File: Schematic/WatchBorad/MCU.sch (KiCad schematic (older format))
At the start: 54 parts, among them J2 Conn_01x07_Female, J3 Conn_01x12, U1 BNO055, U2 nRF52832-QFxx, U3 CAT4002ATD-GT3, U4 MX25R1635F, X1 Crystal_GND24_Small, X2 Crystal_Small, X3 Crystal_Small

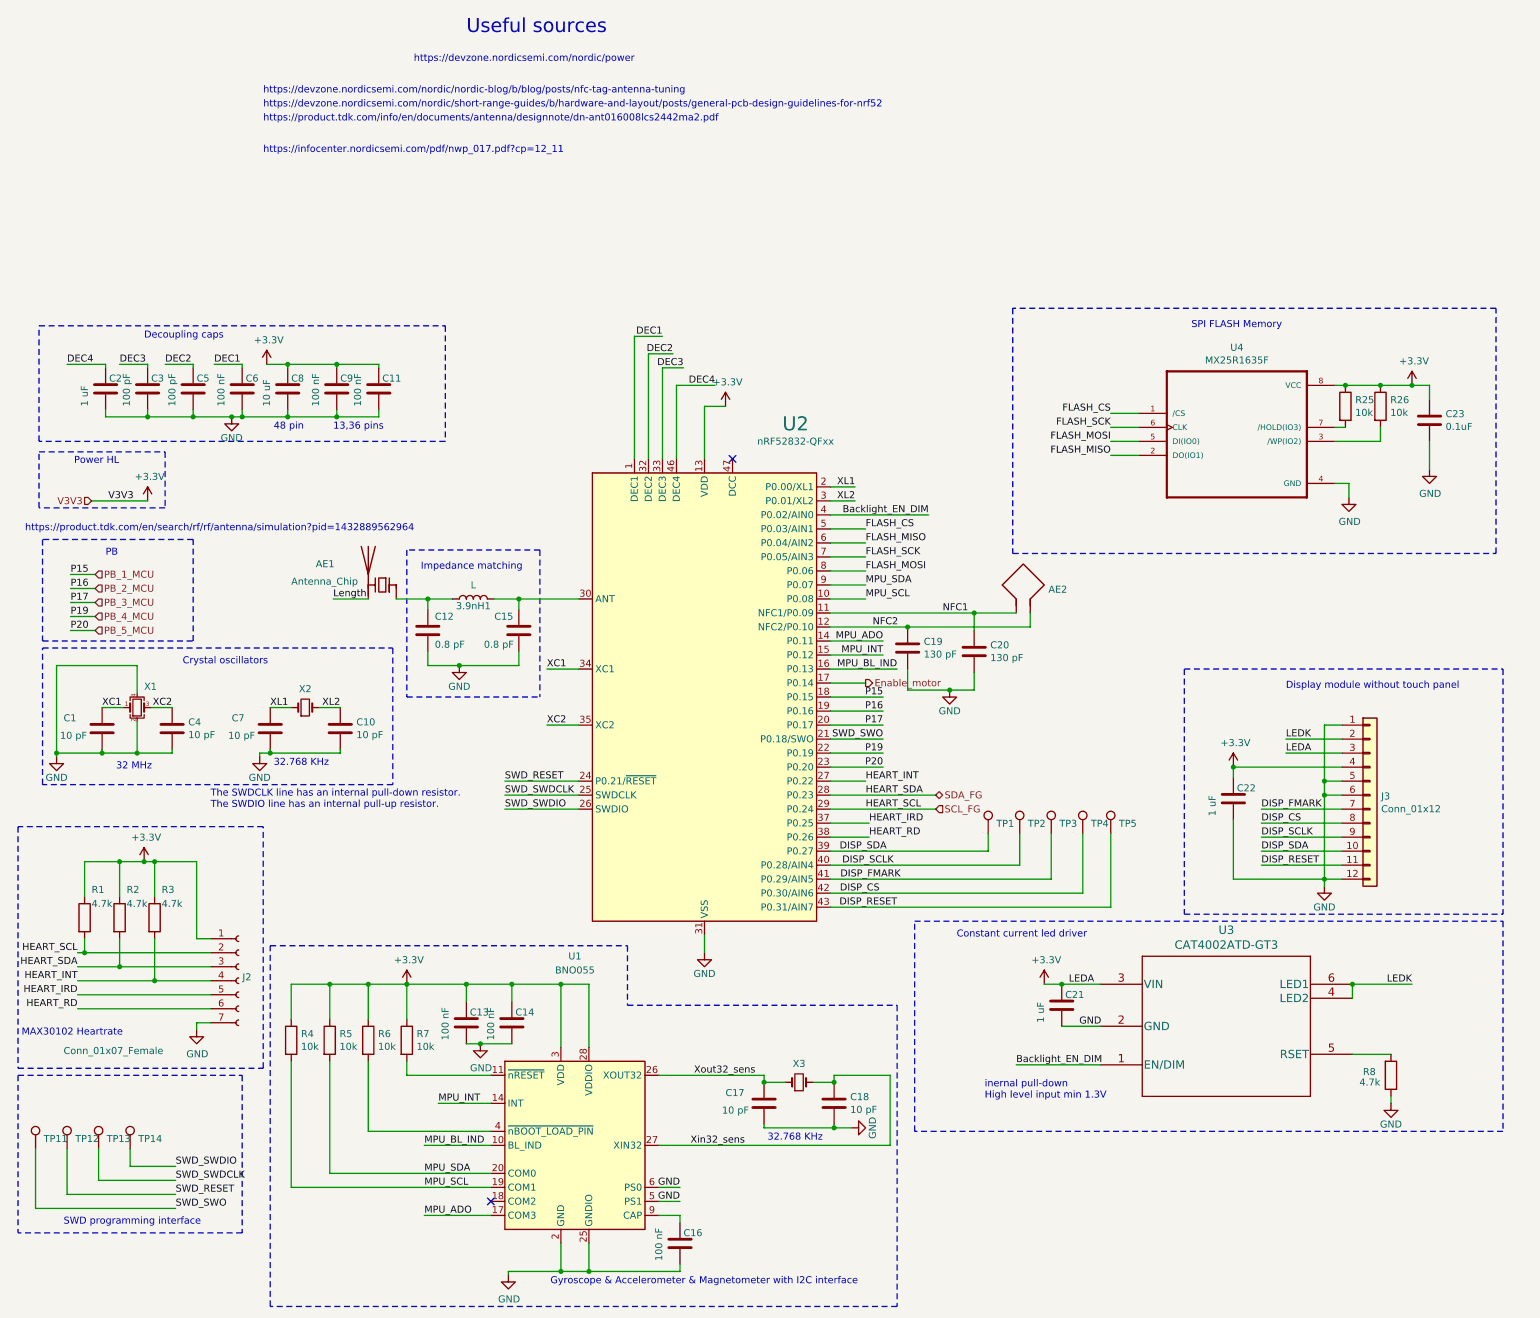
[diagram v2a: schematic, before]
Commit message: PBs are modified to one logic. Some minot changes
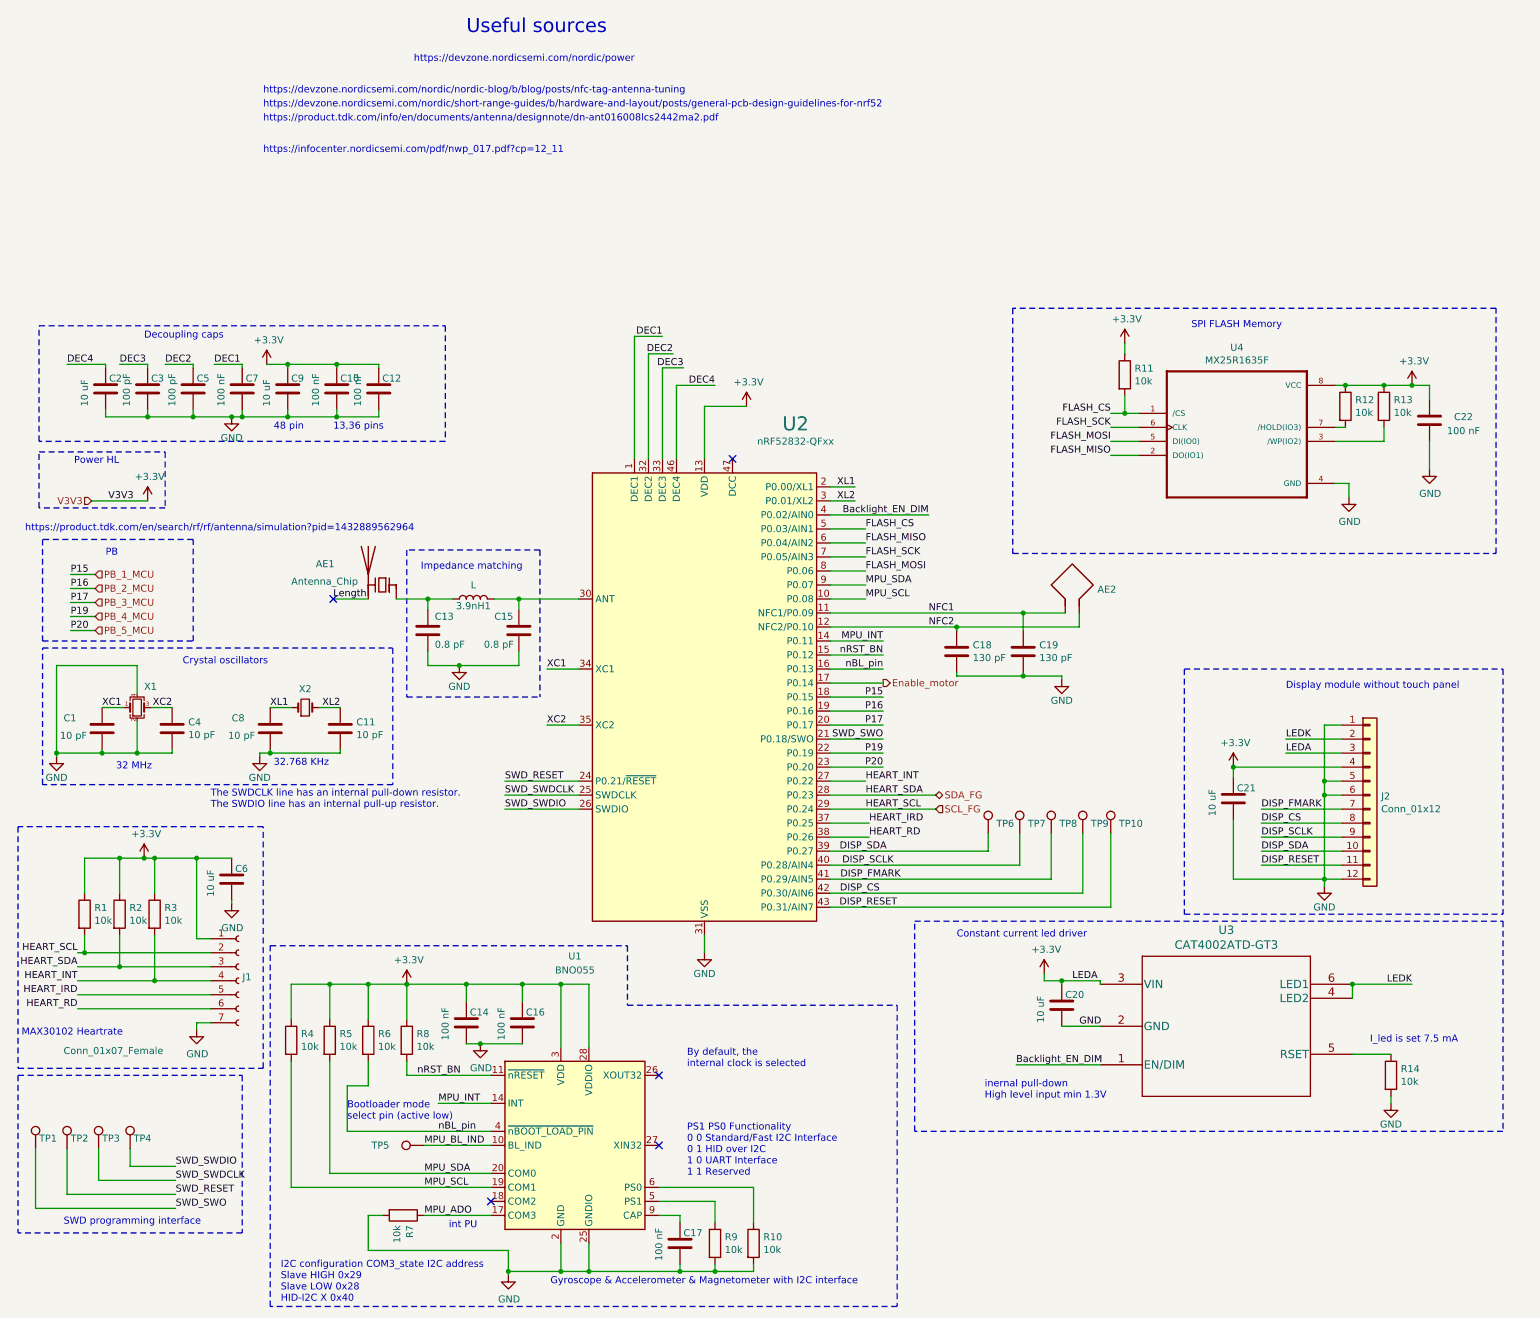
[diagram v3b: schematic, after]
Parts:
- removed C17, C18: 10 pF, Capacitors_SMD:C_0603_HandSoldering, symbol Device:C
- removed C23: 0.1uF, Capacitors_SMD:C_0603_HandSoldering, symbol Device:C
- removed R8: 4.7k, Resistors_SMD:R_0603_HandSoldering, symbol Device:R
- removed X3: Crystal_Small, Crystals:Crystal_SMD_2012-2pin_2.0x1.2mm, symbol Device:Crystal_Small
- added C20, C6: 10 uF, Capacitors_SMD:C_0603_HandSoldering, symbol Device:C
- added R10, R11, R14, R7, R9: 10k, Resistors_SMD:R_0603_HandSoldering, symbol Device:R
- added TP5: TestPoint, Measurement_Points:Measurement_Point_Round-SMD-Pad_Small, symbol Connector:TestPoint
- C2, C21: value 1 uF -> 10 uF; LCSC https://lcsc.com/product-detail/Multilayer-Ceramic-Capacitors-MLCC-SMD-SMT_SANYEAR-C0603X5R105K160NT_C475249.html -> https://lcsc.com/product-detail/Multilayer-Ceramic-Capacitors-MLCC-SMD-SMT_SANYEAR-C0603X5R106M160NT_C466781.html
- C22: value 1 uF -> 100 nF; LCSC https://lcsc.com/product-detail/Multilayer-Ceramic-Capacito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 -> (none)
- R1, R2, R3: value 4.7k -> 10k
- renumbered C9 to C10, C10 to C11, C11 to C12, C12 to C13, C13 to C14, C14 to C16, C16 to C17, C19 to C18, C20 to C19, C6 to C7, C7 to C8, C8 to C9, J2 to J1, J3 to J2, R25 to R12, R26 to R13, R7 to R8, TP11 to TP1, TP5 to TP10, TP12 to TP2, TP13 to TP3, TP14 to TP4, TP1 to TP6, TP2 to TP7, TP3 to TP8, TP4 to TP9
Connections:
- net +3V3: now also C20.1, C6.1, R11.1
- net FLASH_CS: now also R11.2
- net GND: now also C20.2, C6.2, R10.2, R14.2, R7.2, R9.2; no longer U1.5 (PS1), U1.6 (PS0)
- net MPU_ADO: now also R7.1; no longer U2.14 (P0.11)
- net MPU_BL_IND: now also TP5.1; no longer U2.16 (P0.13)
- net MPU_INT: now also U2.14 (P0.11); no longer U2.15 (P0.12)
- net at U3.5 (RSET): now also R14.1
- net nRST_BN: now reaches R8.2, U1.11 (~nRESET)
- net nRST_BN: now also U2.15 (P0.12)
- net nBL_pin: now reaches R6.2, U1.4 (~nBOOT_LOAD_PIN)
- net nBL_pin: now also U2.16 (P0.13)
- net Xin32_sens: no longer names the net of U1.27 (XIN32)
- net Xout32_sens: no longer names the net of U1.26 (XOUT32)
- new net: R9.1, U1.5 (PS1)
- new net: R10.1, U1.6 (PS0)
- no-connect marks 2 -> 5
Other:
- note added: "Bootloader mode\nselect pin (active low)"
- note added: "By default, the\ninternal clock is selected"
- note added: "I2C configuration COM3_state I2C address\nSlave HIGH 0x29\nSlave LOW 0x28\nHID-I2C X 0x40\n"
- note added: "I_led is set 7.5 mA"
- note added: "PS1 PS0 Functionality\n0 0 Standard/Fast I2C Interface\n0 1 HID over I2C\n1 0 UART Interface\n1 1 Reserved"
- note added: "int PU"
- moved on the sheet: AE2, C16, C18, C19, R13

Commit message: Fixed LCSC schematic link :Schematic [SCHEMATIC]
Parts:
- C2, C20, C21, C6, C9: LCSC https://lcsc.com/product-detail/Multilayer-Ceramic-Capacito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 -> (none); lcsc (none) -> https://lcsc.com/product-detail/Multilayer-Ceramic-Capacito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
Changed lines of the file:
@@
 F 2 "Capacitors_SMD:C_0603_HandSoldering" H 2513 1000 50  0001 C CNN
 F 3 "~" H 2475 1150 50  0001 C CNN
-F 4 "https://lcsc.com/product-detail/Multilayer-Ceramic-Capacitors-MLCC-SMD-SMT_SANYEAR-C0603X5R106M160NT_C466781.html" H 2475 1150 50  0001 C CNN "LCSC"
+F 4 "" H 2475 1150 50  0001 C CNN "LCSC"
+F 5 "https://lcsc.com/product-detail/Multilayer-Ceramic-Capacitors-MLCC-SMD-SMT_SANYEAR-C0603X5R106M160NT_C466781.html" H 2475 1150 50  0001 C CNN "lcsc"
 	1    2475 1150
 	1    0    0    -1
@@
 F 2 "Capacitors_SMD:C_0603_HandSoldering" H 1213 1000 50  0001 C CNN
 F 3 "~" H 1175 1150 50  0001 C CNN
-F 4 "https://lcsc.com/product-detail/Multilayer-Ceramic-Capacitors-MLCC-SMD-SMT_SANYEAR-C0603X5R106M160NT_C466781.html" H 1175 1150 50  0001 C CNN "LCSC"
+F 4 "" H 1175 1150 50  0001 C CNN "LCSC"
+F 5 "https://lcsc.com/product-detail/Multilayer-Ceramic-Capacitors-MLCC-SMD-SMT_SANYEAR-C0603X5R106M160NT_C466781.html" H 1175 1150 50  0001 C CNN "lcsc"
 	1    1175 1150
 	1    0    0    -1
@@
 F 2 "Capacitors_SMD:C_0603_HandSoldering" H 9263 3925 50  0001 C CNN
 F 3 "~" H 9225 4075 50  0001 C CNN
-F 4 "https://lcsc.com/product-detail/Multilayer-Ceramic-Capacitors-MLCC-SMD-SMT_SANYEAR-C0603X5R106M160NT_C466781.html" H 9225 4075 50  0001 C CNN "LCSC"
+F 4 "" H 9225 4075 50  0001 C CNN "LCSC"
+F 5 "https://lcsc.com/product-detail/Multilayer-Ceramic-Capacitors-MLCC-SMD-SMT_SANYEAR-C0603X5R106M160NT_C466781.html" H 9225 4075 50  0001 C CNN "lcsc"
 	1    9225 4075
 	1    0    0    -1
@@
 F 2 "Capacitors_SMD:C_0603_HandSoldering" H 8038 5400 50  0001 C CNN
 F 3 "~" H 8000 5550 50  0001 C CNN
-F 4 "https://lcsc.com/product-detail/Multilayer-Ceramic-Capacitors-MLCC-SMD-SMT_SANYEAR-C0603X5R106M160NT_C466781.html" H 8000 5550 50  0001 C CNN "LCSC"
+F 4 "" H 8000 5550 50  0001 C CNN "LCSC"
+F 5 "https://lcsc.com/product-detail/Multilayer-Ceramic-Capacitors-MLCC-SMD-SMT_SANYEAR-C0603X5R106M160NT_C466781.html" H 8000 5550 50  0001 C CNN "lcsc"
 	1    8000 5550
 	1    0    0    -1
@@
 F 2 "Capacitors_SMD:C_0603_HandSoldering" H 2113 4500 50  0001 C CNN
 F 3 "~" H 2075 4650 50  0001 C CNN
-F 4 "https://lcsc.com/product-detail/Multilayer-Ceramic-Capacitors-MLCC-SMD-SMT_SANYEAR-C0603X5R106M160NT_C466781.html" H 2075 4650 50  0001 C CNN "LCSC"
+F 4 "" H 2075 4650 50  0001 C CNN "LCSC"
+F 5 "https://lcsc.com/product-detail/Multilayer-Ceramic-Capacitors-MLCC-SMD-SMT_SANYEAR-C0603X5R106M160NT_C466781.html" H 2075 4650 50  0001 C CNN "lcsc"
 	1    2075 4650
 	1    0    0    -1

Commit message: Added footpring for GC9A01 display. Fixed display lines(FMARK->DC)
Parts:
- removed J2: Conn_01x12, symbol Connector_Generic:Conn_01x12
- added U11: GC9A01, LocalFootprints:GC9A01_disp, symbol GC9A01:GC9A01
- U1: symbol Sensor_Motion:BNO055 -> WatchBorad-rescue:BNO055-Sensor_Motion
- X1: symbol Device:Crystal_GND24_Small -> WatchBorad-rescue:Crystal_GND24_Small-Device
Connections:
- net +3V3: now also U11.3 (LEDA), U11.4 (VDD)
- net DISP_CS: now also U11.8 (CS)
- net DISP_RESET: now also U11.11 (RESET)
- net DISP_SCLK: now also U11.9 (SCL)
- net DISP_SDA: now also U11.10 (SDA)
- net GND: now also U11.1 (GND), U11.12 (GND), U11.5 (GND), U11.6 (GND)
- net LEDK: now also U11.2 (LEDK)
- net DISP_FMARK renamed DISP_DC
- net DISP_DC: now also U11.7 (D/C)
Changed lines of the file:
@@
 	1400 3525 1400 3750
 $Comp
-L Device:Crystal_GND24_Small X1
+L WatchBorad-rescue:Crystal_GND24_Small-Device X1
 U 1 1 5EAD6468
 P 1400 3425
@@
 Text Label 6825 4850 2    50   ~ 0
 DISP_RESET
-Text Label 6850 4650 2    50   ~ 0
-DISP_FMARK
 Text Label 7050 2050 2    50   ~ 0
 Backlight_EN_DIM
@@
 	6350 2950 6725 2950
 $Comp
-L Sensor_Motion:BNO055 U?
+L WatchBorad-rescue:BNO055-Sensor_Motion U?
 U 1 1 5F46C7F5
 P 4525 6550
@@
 DISP_SCLK
 Text Label 9425 4150 0    50   ~ 0
-DISP_FMARK
+DISP_DC
 Wire Wire Line
 	9425 4150 10000 4150
@@
 Text Notes 9600 3300 0    50   ~ 0
 Display module without touch panel\n
-$Comp
-L Connector_Generic:Conn_01x12 J2
-U 1 1 5F7CA256
-P 10200 4050
-F 0 "J2" H 10280 4042 50  0000 L CNN
-F 1 "Conn_01x12" H 10280 3951 50  0000 L CNN
-F 2 "" H 10200 4050 50  0001 C CNN
-F 3 "https://www.buydisplay.com/download/manual/ER-TFT1.28-1_Datasheet.pdf" H 10200 4050 50  0001 C CNN
-	1    10200 4050
-	1    0    0    -1
-$EndComp
 $Comp
 L power:GND #PWR?
@@
 LEDA
 NoConn ~ 2800 2650
+$Comp
+L GC9A01:GC9A01 U11
+U 1 1 60CF55BA
+P 10250 4050
+F 0 "U11" H 10428 4046 50  0000 L CNN
+F 1 "GC9A01" H 10428 3955 50  0000 L CNN
+F 2 "LocalFootprints:GC9A01_disp" H 10000 4400 50  0001 C CNN
+F 3 "https://www.buydisplay.com/download/ic/GC9A01A.pdf" H 10000 4400 50  0001 C CNN
+	1    10250 4050
+	1    0    0    -1
+$EndComp
+Text Label 6700 4650 2    50   ~ 0
+DISP_DC
 $EndSCHEMATC

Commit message: Fixed components references for 0603 resistors and capacitors[SCHEMATIC]
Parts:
- 3.9nH1, AE1, C1, C10, C11, C12, C13, C14, C15, C16, C17, C18, C19, C2, C20, C21, C22, C3, C4, C5, C6, C7, C8, C9: footprint Capacitors_SMD:C_0603_HandSoldering -> Capacitor_SMD:C_0603_1608Metric_Pad1.08x0.95mm_HandSolder
- R1, R10, R11, R12, R13, R14, R2, R3, R4, R5, R6, R7, R8, R9: footprint Resistors_SMD:R_0603_HandSoldering -> Resistor_SMD:R_0603_1608Metric_Pad0.98x0.95mm_HandSolder

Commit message: Updated 0603 components from hand-solder version to fabrical
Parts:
- 3.9nH1, AE1, C1, C10, C11, C12, C13, C14, C15, C16, C17, C18, C19, C2, C20, C21, C22, C3, C4, C5, C6, C7, C8, C9: footprint Capacitor_SMD:C_0603_1608Metric_Pad1.08x0.95mm_HandSolder -> Capacitor_SMD:C_0603_1608Metric
- R1, R10, R11, R12, R13, R14, R2, R3, R4, R5, R6, R7, R8, R9: footprint Resistor_SMD:R_0603_1608Metric_Pad0.98x0.95mm_HandSolder -> Resistor_SMD:R_0603_1608Metric

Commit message: Added winbond flash instead of previous one
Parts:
- U4: footprint SMD_Packages:SOIC-8-N -> LocalFootprints:W25Q128JVPIQ
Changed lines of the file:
@@
 Text Notes 8925 725  0    50   ~ 0
 SPI FLASH Memory\n
-$Comp
-L W25Q16BVSSIG:MX25R1635F U?
-U 1 1 5ECE6AE0
-P 9250 1525
-AR Path="/5ECE6AE0" Ref="U?"  Part="1"
-AR Path="/5E9B1DCE/5ECE6AE0" Ref="U4"  Part="1"
-F 0 "U4" H 9250 2195 50  0000 C CNN
-F 1 "MX25R1635F" H 9250 2104 50  0000 C CNN
-F 2 "SMD_Packages:SOIC-8-N" H 9250 1525 50  0001 L BNN
-F 3 "https://datasheet.lcsc.com/szlcsc/Macronix-MX25R1635FM2IL0_C152602.pdf" H 9250 1525 50  0001 L BNN
-F 4 "https://lcsc.com/product-detail/FLASH_MXIC-Macronix-MX25R1635FM2IL0_C152602.html" H 9250 1525 50  0001 C CNN "lcsc"
-	1    9250 1525
-	1    0    0    -1
-$EndComp
 Text Label 6600 2150 0    50   ~ 0
 FLASH_CS
@@
 Text Label 6700 4650 2    50   ~ 0
 DISP_DC
+$Comp
+L W25Q16BVSSIG:MX25R1635F U?
+U 1 1 5ECE6AE0
+P 9250 1525
+AR Path="/5ECE6AE0" Ref="U?"  Part="1"
+AR Path="/5E9B1DCE/5ECE6AE0" Ref="U4"  Part="1"
+F 0 "U4" H 9250 2195 50  0000 C CNN
+F 1 "MX25R1635F" H 9250 2104 50  0000 C CNN
+F 2 "LocalFootprints:W25Q128JVPIQ" H 9250 1525 50  0001 L BNN
+F 3 "https://datasheet.lcsc.com/szlcsc/Macronix-MX25R1635FM2IL0_C152602.pdf" H 9250 1525 50  0001 L BNN
+F 4 "https://lcsc.com/product-detail/FLASH_MXIC-Macronix-MX25R1635FM2IL0_C152602.html" H 9250 1525 50  0001 C CNN "lcsc"
+	1    9250 1525
+	1    0    0    -1
+$EndComp
 $EndSCHEMATC
